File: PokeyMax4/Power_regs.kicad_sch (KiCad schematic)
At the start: 4 parts

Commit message: Update the v4 board
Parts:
- C8: JLCPCB Part # C452745 -> (none); LCSC Part # (none) -> C12530
- C9: JLCPCB Part # C23733 -> (none); LCSC Part # (none) -> C23733
- L1: JLCPCB Part # C171753 -> (none); LCSC Part # (none) -> C20616175
- REG1: JLCPCB Part # C398923 -> (none); LCSC Part # (none) -> C398923

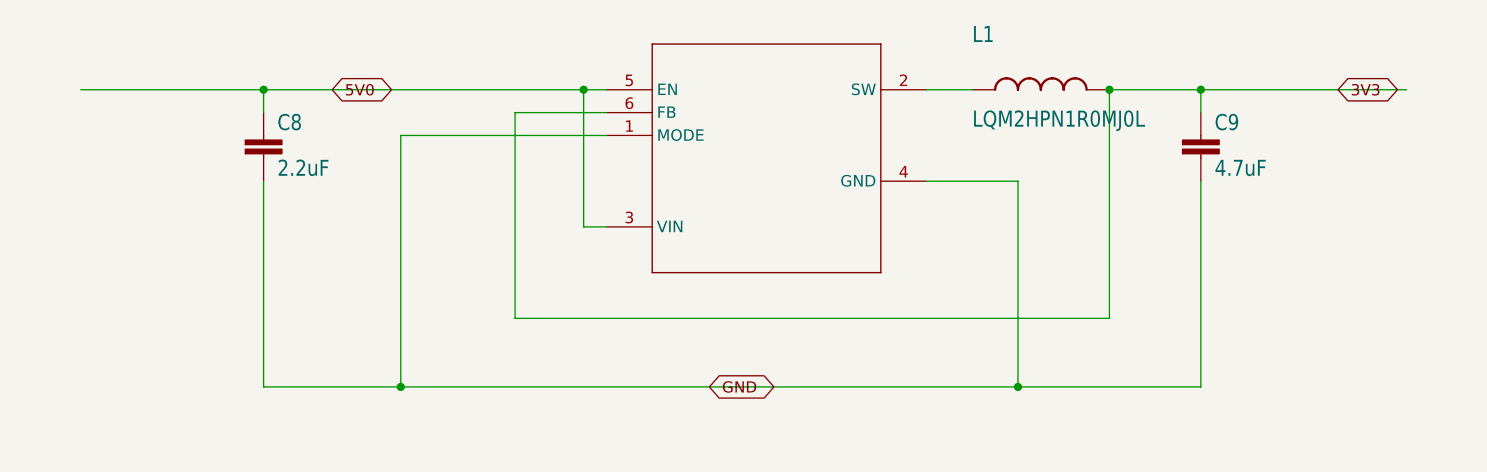
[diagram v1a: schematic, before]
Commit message: Updates for JLCPCB fabrication and parts library
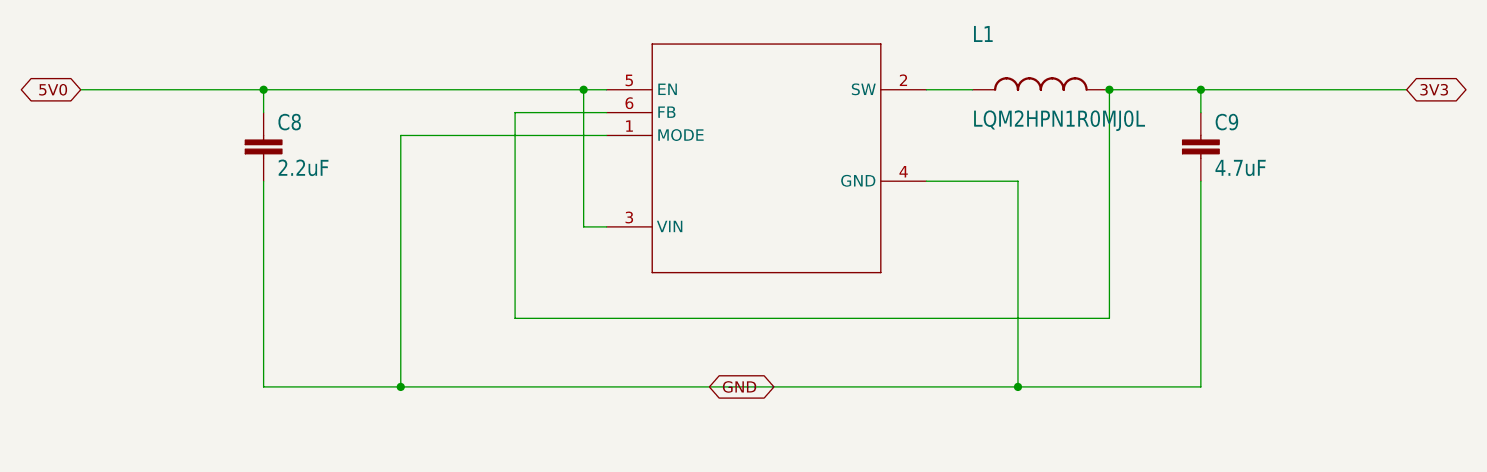
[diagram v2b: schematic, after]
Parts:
- L1: LCSC Part # C20616175 -> C216157
- REG1: JLCPCB Rotation Offset (none) -> 270
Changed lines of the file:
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@@
 	(global_label "3V3"
 		(shape bidirectional)
-		(at 213.36 91.44 0)
+		(at 220.98 91.44 0)
 		(fields_autoplaced yes)
 		(effects
@@
 		)
 		(property "Intersheetrefs" "${INTERSHEET_REFS}"
-			(at 220.8116 91.44 0)
+			(at 228.4316 91.44 0)
 			(effects
 				(font
@@
 	(global_label "5V0"
 		(shape bidirectional)
-		(at 101.6 91.44 0)
+		(at 73.66 91.44 180)
 		(fields_autoplaced yes)
 		(effects
@@
 				(size 1.2446 1.2446)
 			)
-			(justify left)
+			(justify right)
 		)
 		(property "Intersheetrefs" "${INTERSHEET_REFS}"
-			(at 109.0516 91.44 0)
+			(at 81.1116 91.44 0)
 			(effects
 				(font
@@
 			)
 		)
-		(property "LCSC Part #" "C20616175"
+		(property "LCSC Part #" "C216157"
+			(at 180.34 91.44 0)
+			(effects
+				(font
+					(size 1.27 1.27)
+				)
+				(hide yes)
+			)
+		)
+		(property "JLCPCB Rotation Offset" ""
 			(at 180.34 91.44 0)
 			(effects
@@
 			)
 		)
+		(property "JLCPCB Rotation Offset" ""
+			(at 93.98 96.52 0)
+			(effects
+				(font
+					(size 1.27 1.27)
+				)
+				(hide yes)
+			)
+		)
 		(pin "1"
 		)
@@
 			)
 		)
+		(property "JLCPCB Rotation Offset" "270"
+			(at 129.54 91.44 0)
+			(effects
+				(font
+					(size 1.27 1.27)
+				)
+				(hide yes)
+			)
+		)
 		(pin "3"
 		)
@@
 			(at 198.12 96.52 0)
 			(effects
+				(font
+					(size 1.27 1.27)
+				)
+				(hide yes)
+			)
+		)
+		(property "JLCPCB Rotation Offset" ""
+			(at 198.12 96.52 0)
+			(effects

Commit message: Update BOM from 0402 to 0603 where relevant
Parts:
- C8: LCSC Part # C12530 -> C43922
- C9: LCSC Part # C23733 -> C112433
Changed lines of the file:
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@@
 			)
 		)
-		(property "LCSC Part #" "C12530"
+		(property "LCSC Part #" "C43922"
 			(at 93.98 96.52 0)
 			(effects
@@
 			)
 		)
-		(property "LCSC Part #" " C23733"
+		(property "LCSC Part #" "C112433"
 			(at 198.12 96.52 0)
 			(effects
